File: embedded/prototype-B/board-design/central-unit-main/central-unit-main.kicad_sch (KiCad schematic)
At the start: 0 parts

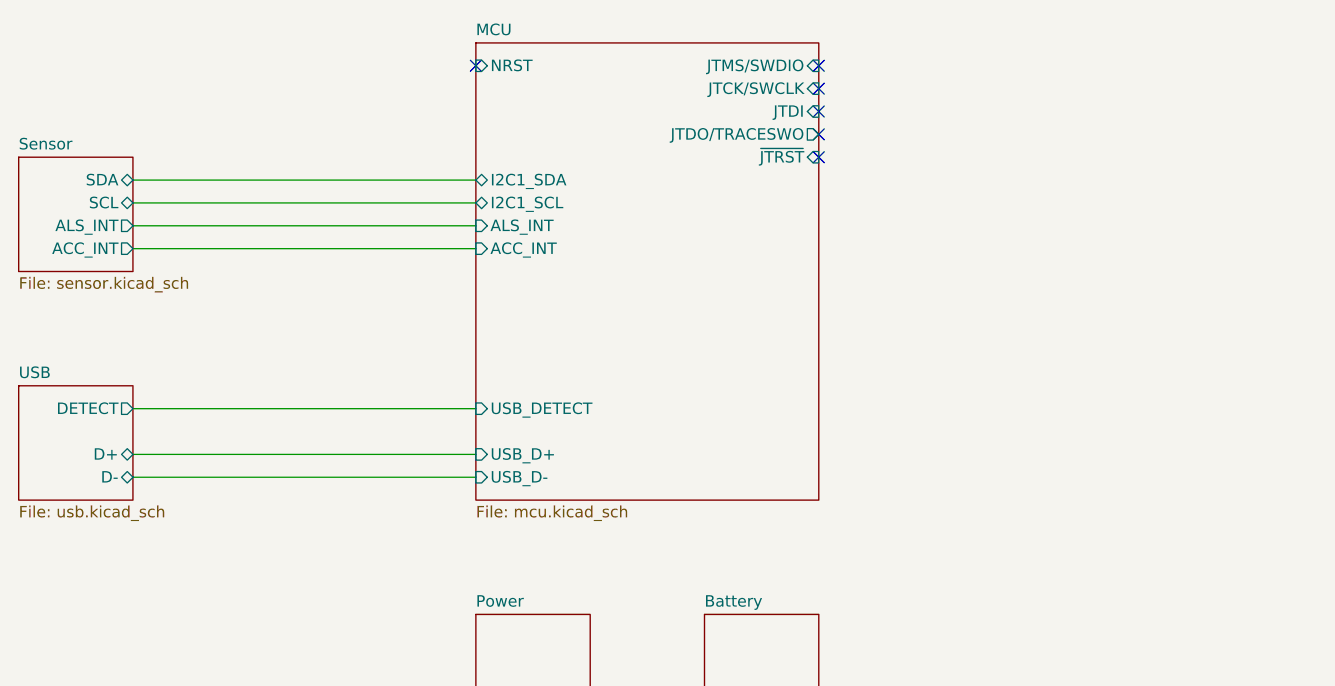
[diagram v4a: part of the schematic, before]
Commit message: [Central unit] Connectors
Two types of connectors have been implemented for this iteration. 20-pin
JTAG connector for debugging and 2 I2C/SPI compatible 2x5 2.54mm
connectors for lighting peripherals.

Signed-off-by: Nicolae-Andrei Vasile <vasilenicolaeandrei@gmail.com>
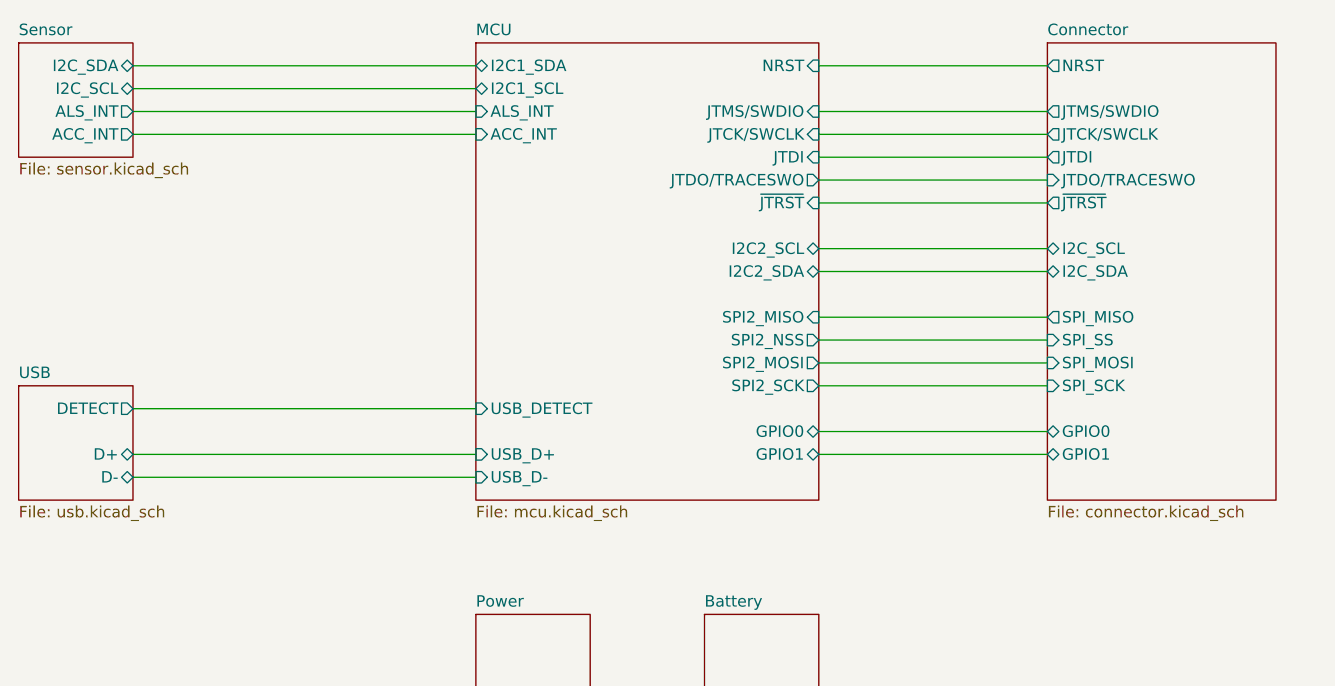
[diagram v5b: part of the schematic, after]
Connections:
- no-connect marks 6 -> 0
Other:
- added sheet Connector (connector.kicad_sch)
- sheet MCU ports: added GPIO0, GPIO1, I2C2_SCL, I2C2_SDA, SPI2_MISO, SPI2_MOSI, SPI2_NSS, SPI2_SCK; removed none
- sheet Sensor ports: added I2C_SCL, I2C_SDA; removed SCL, SDA
